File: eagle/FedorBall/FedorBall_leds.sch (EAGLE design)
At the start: 8 parts, among them U1 TLC5940-NT, U2 TLC5940-NT, U3 TLC5940-NT, U4 TLC5940-NT

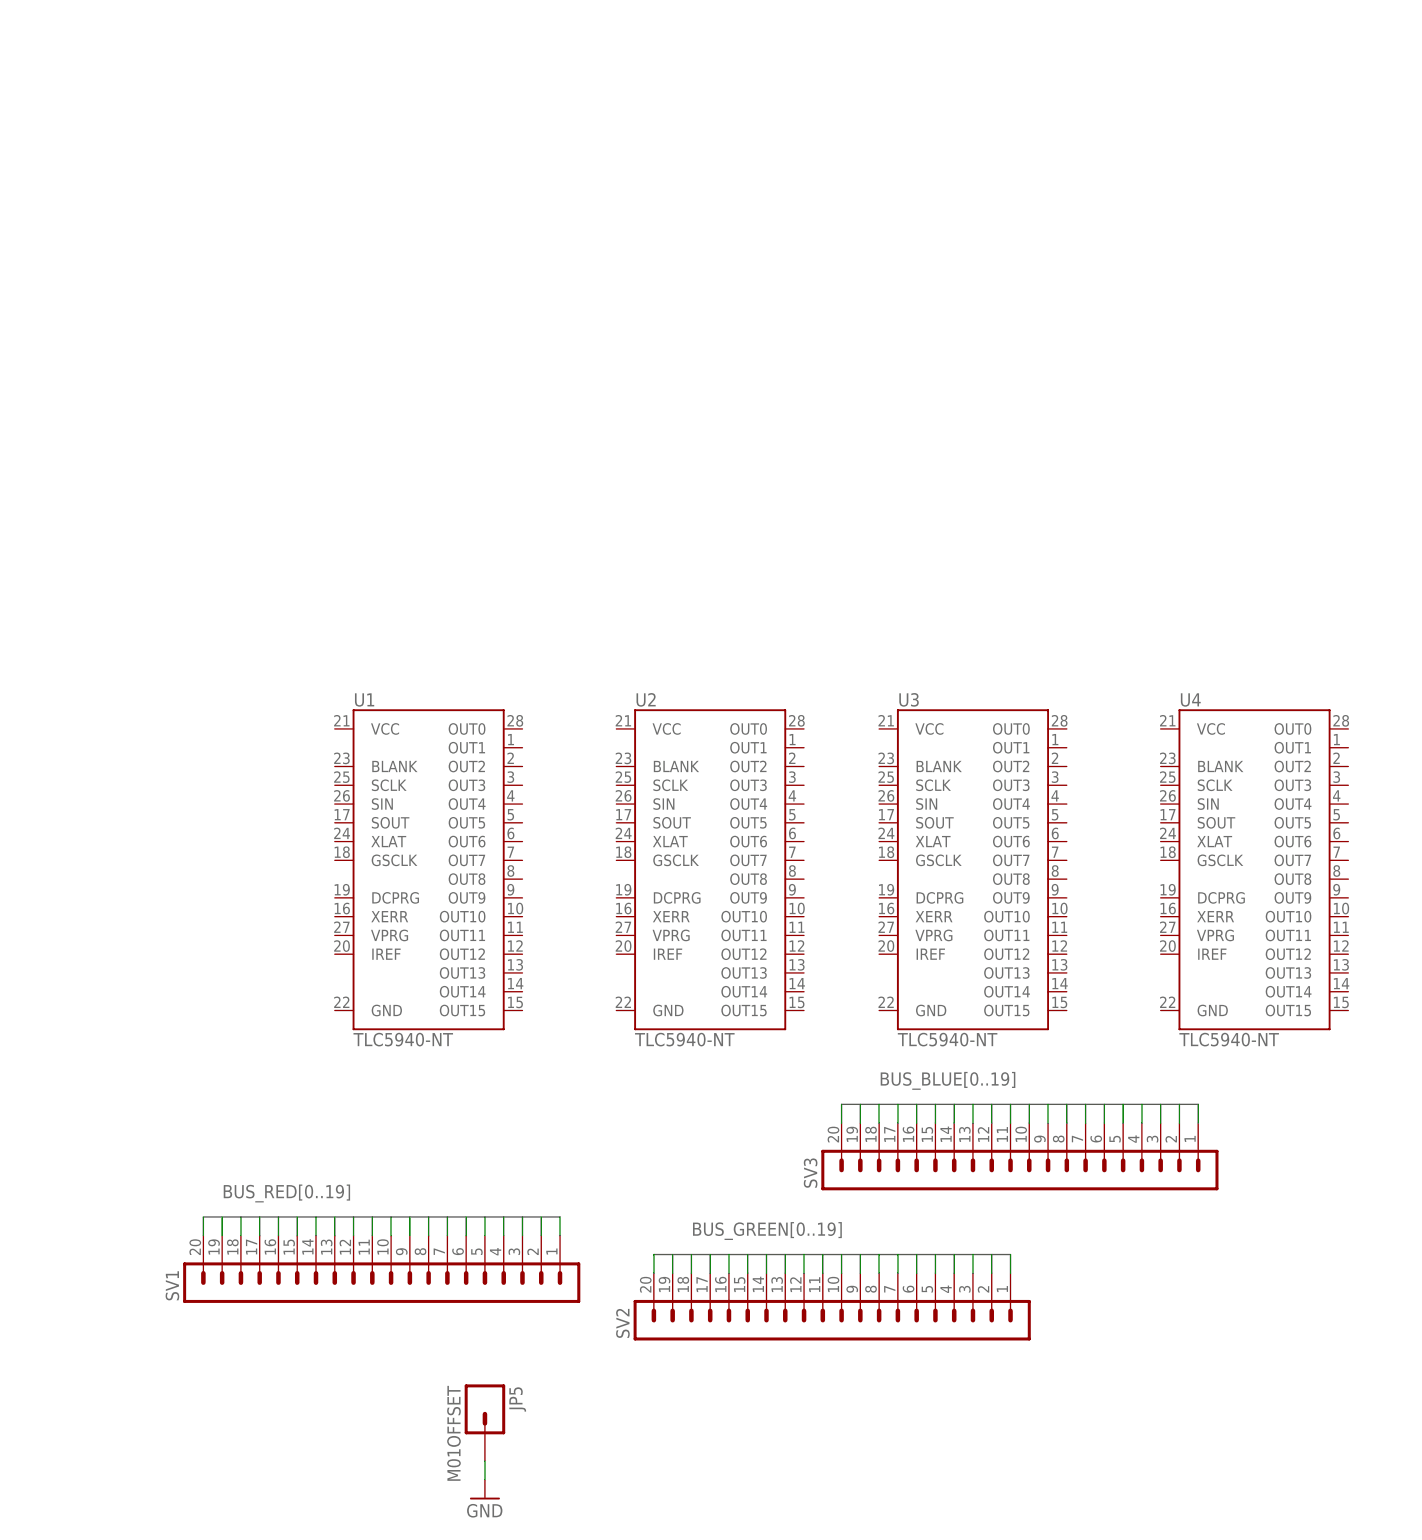
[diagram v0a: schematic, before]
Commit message: continue implementing leds driver scheme
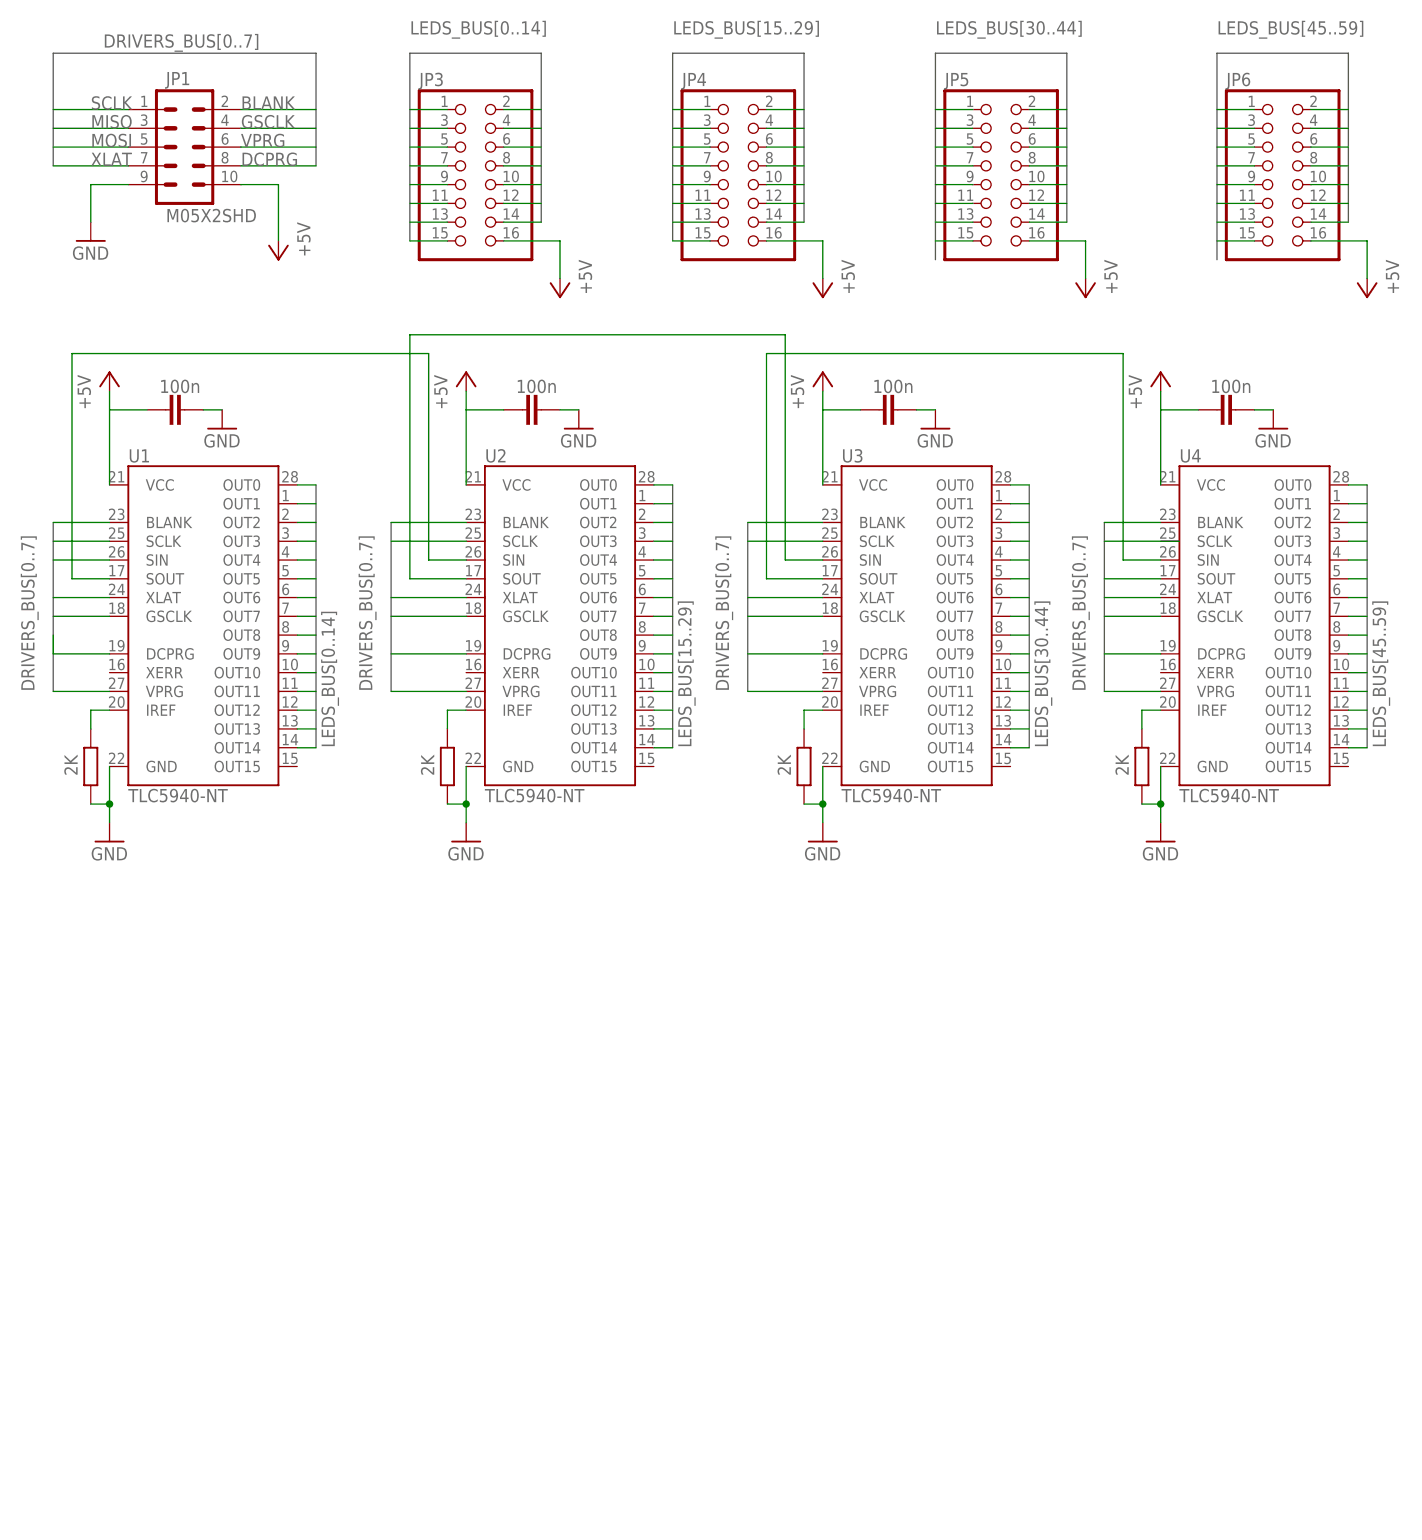
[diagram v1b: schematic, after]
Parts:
- removed SV1, SV2, SV3: (no value), con-lstb:MA20-1L
- added C1, C2, C3, C4: 100n, rcl:C-EU025-024X044
- added JP1: M05X2SHD, SparkFun:M05X2SHD
- added JP3, JP4, JP6: (no value), pinhead:PINHD-2X8
- added R1, R2, R3, R4: 2K, resistor:R-EU_0204/5
- JP5: value M01OFFSET -> (none); device SparkFun:M01OFFSET -> pinhead:PINHD-2X8
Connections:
- removed net BUS_BLUE0: SV3.1
- removed net BUS_BLUE1: SV3.2
- removed net BUS_BLUE10: SV3.11
- removed net BUS_BLUE11: SV3.12
- removed net BUS_BLUE12: SV3.13
- removed net BUS_BLUE13: SV3.14
- removed net BUS_BLUE14: SV3.15
- removed net BUS_BLUE15: SV3.16
- removed net BUS_BLUE16: SV3.17
- removed net BUS_BLUE17: SV3.18
- removed net BUS_BLUE18: SV3.19
- removed net BUS_BLUE19: SV3.20
- removed net BUS_BLUE2: SV3.3
- removed net BUS_BLUE3: SV3.4
- removed net BUS_BLUE4: SV3.5, SV3.6
- removed net BUS_BLUE6: SV3.7
- removed net BUS_BLUE7: SV3.8
- removed net BUS_BLUE8: SV3.9
- removed net BUS_BLUE9: SV3.10
- removed net BUS_GREEN0: SV2.1
- removed net BUS_GREEN1: SV2.2
- removed net BUS_GREEN10: SV2.11
- removed net BUS_GREEN11: SV2.12
- removed net BUS_GREEN12: SV2.13
- removed net BUS_GREEN13: SV2.14
- removed net BUS_GREEN14: SV2.15
- removed net BUS_GREEN15: SV2.16
- removed net BUS_GREEN16: SV2.17
- removed net BUS_GREEN17: SV2.18
- removed net BUS_GREEN18: SV2.19
- removed net BUS_GREEN19: SV2.20
- removed net BUS_GREEN3: SV2.3, SV2.4
- removed net BUS_GREEN4: SV2.5
- removed net BUS_GREEN5: SV2.6
- removed net BUS_GREEN6: SV2.7
- removed net BUS_GREEN7: SV2.8
- removed net BUS_GREEN8: SV2.9
- removed net BUS_GREEN9: SV2.10
- removed net BUS_RED0: SV1.1
- removed net BUS_RED1: SV1.2
- removed net BUS_RED10: SV1.11
- removed net BUS_RED11: SV1.12
- removed net BUS_RED12: SV1.13
- removed net BUS_RED13: SV1.14
- removed net BUS_RED14: SV1.15
- removed net BUS_RED15: SV1.16
- removed net BUS_RED16: SV1.17
- removed net BUS_RED17: SV1.18
- removed net BUS_RED18: SV1.19
- removed net BUS_RED19: SV1.20
- removed net BUS_RED2: SV1.3
- removed net BUS_RED3: SV1.4
- removed net BUS_RED4: SV1.5
- removed net BUS_RED5: SV1.6
- removed net BUS_RED6: SV1.7
- removed net BUS_RED7: SV1.8
- removed net BUS_RED8: SV1.9
- removed net BUS_RED9: SV1.10
- new net +5V: C1.1, C2.1, C3.1, C4.1, JP1.10, JP3.16, JP4.16, JP5.16, JP6.16, U1.VCC, U2.VCC, U3.VCC, U4.VCC
- new net DRIVERS_BUS0: JP1.2, U1.BLANK, U2.BLANK, U3.BLANK, U4.BLANK
- new net DRIVERS_BUS1: JP1.1, U1.SCLK, U2.SCLK, U3.SCLK
- new net DRIVERS_BUS2: JP1.5, U1.SIN
- new net DRIVERS_BUS3: JP1.3, U4.SOUT
- new net DRIVERS_BUS4: JP1.7, U1.XLAT, U2.XLAT, U3.XLAT, U4.XLAT
- new net DRIVERS_BUS5: JP1.4, U1.GSCLK, U2.GSCLK, U3.GSCLK, U4.GSCLK
- new net DRIVERS_BUS6: JP1.8, U1.DCPRG, U2.DCPRG, U3.DCPRG, U4.DCPRG
- new net DRIVERS_BUS7: JP1.6, U1.VPRG, U2.VPRG, U3.VPRG, U4.VPRG
- new net LEDS_BUS0: JP3.1, U1.OUT0
- new net LEDS_BUS1: JP3.3, U1.OUT1
- new net LEDS_BUS10: JP3.6, U1.OUT10
- new net LEDS_BUS11: JP3.8, U1.OUT11
- new net LEDS_BUS12: JP3.10, U1.OUT12
- new net LEDS_BUS13: JP3.12, U1.OUT13
- new net LEDS_BUS14: JP3.14, U1.OUT14
- new net LEDS_BUS15: JP4.1, U2.OUT0
- new net LEDS_BUS16: JP4.3, U2.OUT1
- new net LEDS_BUS17: JP4.5, U2.OUT2
- new net LEDS_BUS18: JP4.7, U2.OUT3
- new net LEDS_BUS19: JP4.9, U2.OUT4
- new net LEDS_BUS2: JP3.5, U1.OUT2
- new net LEDS_BUS20: JP4.11, U2.OUT5
- new net LEDS_BUS21: JP4.13, U2.OUT6
- new net LEDS_BUS22: JP4.15, U2.OUT7
- new net LEDS_BUS23: JP4.2, U2.OUT8
- new net LEDS_BUS24: JP4.4, U2.OUT9
- new net LEDS_BUS25: JP4.6, U2.OUT10
- new net LEDS_BUS26: JP4.8, U2.OUT11
- new net LEDS_BUS27: JP4.10, U2.OUT12
- new net LEDS_BUS28: JP4.12, U2.OUT13
- new net LEDS_BUS29: JP4.14, U2.OUT14
- new net LEDS_BUS3: JP3.7, U1.OUT3
- new net LEDS_BUS30: JP5.1, U3.OUT0
- new net LEDS_BUS31: JP5.3, U3.OUT1
- new net LEDS_BUS32: JP5.5, U3.OUT2
- new net LEDS_BUS33: JP5.7, U3.OUT3
- new net LEDS_BUS34: JP5.9, U3.OUT4
- new net LEDS_BUS35: JP5.11, U3.OUT5
- new net LEDS_BUS36: JP5.13, U3.OUT6
- new net LEDS_BUS37: JP5.15, U3.OUT7
- new net LEDS_BUS38: JP5.2, U3.OUT8
- new net LEDS_BUS39: JP5.4, U3.OUT9
- new net LEDS_BUS4: JP3.9, U1.OUT4
- new net LEDS_BUS40: JP5.6, U3.OUT10
- new net LEDS_BUS41: JP5.8, U3.OUT11
- new net LEDS_BUS42: JP5.10, U3.OUT12
- new net LEDS_BUS43: JP5.12, U3.OUT13
- new net LEDS_BUS44: JP5.14, U3.OUT14
- new net LEDS_BUS45: JP6.1, U4.OUT0
- new net LEDS_BUS46: JP6.3, U4.OUT1
- new net LEDS_BUS47: JP6.5, U4.OUT2
- new net LEDS_BUS48: JP6.7, U4.OUT3
- new net LEDS_BUS49: JP6.9, U4.OUT4
- new net LEDS_BUS5: JP3.11, U1.OUT5
- new net LEDS_BUS50: JP6.11, U4.OUT5
- new net LEDS_BUS51: JP6.13, U4.OUT6
- new net LEDS_BUS52: JP6.15, U4.OUT7
- new net LEDS_BUS53: JP6.2, U4.OUT8
- new net LEDS_BUS54: JP6.4, U4.OUT9
- new net LEDS_BUS55: JP6.6, U4.OUT10
- new net LEDS_BUS56: JP6.8, U4.OUT11
- new net LEDS_BUS57: JP6.10, U4.OUT12
- new net LEDS_BUS58: JP6.12, U4.OUT13
- new net LEDS_BUS59: JP6.14, U4.OUT14
- new net LEDS_BUS6: JP3.13, U1.OUT6
- new net LEDS_BUS7: JP3.15, U1.OUT7
- new net LEDS_BUS8: JP3.2, U1.OUT8
- new net LEDS_BUS9: JP3.4, U1.OUT9
- new net N$1: U1.SOUT, U2.SIN
- new net N$2: U2.SOUT, U3.SIN
- new net N$3: U3.SOUT, U4.SIN
- new net N$4: R2.2, U1.IREF
- new net N$5: R4.2, U2.IREF
- new net N$6: R3.2, U3.IREF
- new net N$7: R1.2, U4.IREF
- net GND: now also C1.2, C2.2, C3.2, C4.2, JP1.9, R1.1, R2.1, R3.1, R4.1, U1.GND, U2.GND, U3.GND, U4.GND; no longer JP5.1
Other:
- note added: "BLANK"
- note added: "DCPRG"
- note added: "GSCLK"
- note added: "MISO"
- note added: "MOSI"
- note added: "SCLK"
- note added: "VPRG"
- note added: "XLAT"
- moved on the sheet: U1, U2, U3, U4

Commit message: update scheme
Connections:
- net +5V: now also JP1.2; no longer JP1.10
- net DRIVERS_BUS0: now also JP1.6; no longer JP1.2
- net DRIVERS_BUS1: now also JP1.10; no longer JP1.1
- net DRIVERS_BUS2: now also JP1.9; no longer JP1.5
- net DRIVERS_BUS3: now also JP1.8; no longer JP1.3
- net DRIVERS_BUS4: now also JP1.3; no longer JP1.7
- net DRIVERS_BUS5: now also JP1.7; no longer JP1.4
- net DRIVERS_BUS6: now also JP1.4; no longer JP1.8
- net DRIVERS_BUS7: now also JP1.5; no longer JP1.6
- net GND: now also JP1.1; no longer JP1.9
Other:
- note added: "SIN"
- note added: "SOUT"
- note removed: "MISO"
- note removed: "MOSI"
- moved on the sheet: JP1
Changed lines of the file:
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@@
 <part name="P+8" library="supply1" deviceset="+5V" device=""/>
 <part name="P+9" library="supply1" deviceset="+5V" device=""/>
-<part name="P+10" library="supply1" deviceset="+5V" device=""/>
-<part name="GND5" library="supply1" deviceset="GND" device=""/>
 <part name="C1" library="rcl" deviceset="C-EU" device="025-024X044" value="100n"/>
 <part name="C2" library="rcl" deviceset="C-EU" device="025-024X044" value="100n"/>
@@
 <part name="GND8" library="supply1" deviceset="GND" device=""/>
 <part name="GND9" library="supply1" deviceset="GND" device=""/>
+<part name="P+1" library="supply1" deviceset="+5V" device=""/>
+<part name="GND5" library="supply1" deviceset="GND" device=""/>
 </parts>
 <sheets>
 <sheet>
 <plain>
-<text x="-12.7" y="175.26" size="1.778" layer="95">SCLK</text>
-<text x="-12.7" y="172.72" size="1.778" layer="95">MISO</text>
-<text x="-12.7" y="170.18" size="1.778" layer="95">MOSI</text>
-<text x="-12.7" y="167.64" size="1.778" layer="95">XLAT</text>
-<text x="7.62" y="175.26" size="1.778" layer="95">BLANK</text>
-<text x="7.62" y="172.72" size="1.778" layer="95">GSCLK</text>
-<text x="7.62" y="170.18" size="1.778" layer="95">VPRG</text>
+<text x="-15.24" y="167.64" size="1.778" layer="95">XLAT</text>
+<text x="-15.24" y="165.1" size="1.778" layer="95">VPRG</text>
+<text x="-15.24" y="162.56" size="1.778" layer="95">GSCLK</text>
+<text x="-15.24" y="160.02" size="1.778" layer="95">SIN</text>
 <text x="7.62" y="167.64" size="1.778" layer="95">DCPRG</text>
+<text x="7.62" y="165.1" size="1.778" layer="95">BLANK</text>
+<text x="7.62" y="162.56" size="1.778" layer="95">SOUT</text>
+<text x="7.62" y="160.02" size="1.778" layer="95">SCLK</text>
 </plain>
 <instances>
@@
 <instance part="U3" gate="G$1" x="99.06" y="106.68"/>
 <instance part="U4" gate="G$1" x="144.78" y="106.68"/>
-<instance part="JP1" gate="G$1" x="0" y="170.18"/>
+<instance part="JP1" gate="G$1" x="0" y="165.1"/>
 <instance part="JP3" gate="A" x="38.1" y="167.64"/>
 <instance part="JP4" gate="A" x="73.66" y="167.64"/>
@@
 <instance part="P+8" gate="1" x="86.36" y="139.7"/>
 <instance part="P+9" gate="1" x="132.08" y="139.7"/>
-<instance part="P+10" gate="1" x="12.7" y="154.94" rot="R180"/>
-<instance part="GND5" gate="1" x="-12.7" y="157.48"/>
 <instance part="C1" gate="G$1" x="-2.54" y="134.62" smashed="yes" rot="R90">
 <attribute name="VALUE" x="2.159" y="138.684" size="1.778" layer="96" rot="R180"/>
@@
 <instance part="GND8" gate="1" x="101.6" y="132.08"/>
 <instance part="GND9" gate="1" x="147.32" y="132.08"/>
+<instance part="P+1" gate="1" x="17.78" y="182.88"/>
+<instance part="GND5" gate="1" x="-17.78" y="182.88" rot="R180"/>
 </instances>
 <busses>
@@
 <bus name="DRIVERS_BUS[0..7]">
 <segment>
+<wire x1="76.2" y1="119.38" x2="76.2" y2="96.52" width="0.762" layer="92"/>
+<label x="73.66" y="96.52" size="1.778" layer="95" rot="R90"/>
+</segment>
+<segment>
+<wire x1="27.94" y1="119.38" x2="27.94" y2="96.52" width="0.762" layer="92"/>
+<label x="25.4" y="96.52" size="1.778" layer="95" rot="R90"/>
+</segment>
+<segment>
 <wire x1="-17.78" y1="119.38" x2="-17.78" y2="96.52" width="0.762" layer="92"/>
 <label x="-20.32" y="96.52" size="1.778" layer="95" rot="R90"/>
-<wire x1="27.94" y1="119.38" x2="27.94" y2="96.52" width="0.762" layer="92"/>
-<wire x1="76.2" y1="119.38" x2="76.2" y2="96.52" width="0.762" layer="92"/>
+</segment>
+<segment>
 <wire x1="124.46" y1="119.38" x2="124.46" y2="96.52" width="0.762" layer="92"/>
-<label x="25.4" y="96.52" size="1.778" layer="95" rot="R90"/>
-<label x="73.66" y="96.52" size="1.778" layer="95" rot="R90"/>
 <label x="121.92" y="96.52" size="1.778" layer="95" rot="R90"/>
-<label x="10.16" y="185.42" size="1.778" layer="95" rot="R180"/>
-<wire x1="-17.78" y1="167.64" x2="-17.78" y2="182.88" width="0.762" layer="92"/>
-<wire x1="-17.78" y1="182.88" x2="17.78" y2="182.88" width="0.762" layer="92"/>
-<wire x1="17.78" y1="182.88" x2="17.78" y2="167.64" width="0.762" layer="92"/>
+</segment>
+<segment>
+<wire x1="-17.78" y1="167.64" x2="-17.78" y2="154.94" width="0.762" layer="92"/>
+<wire x1="-17.78" y1="154.94" x2="17.78" y2="154.94" width="0.762" layer="92"/>
+<wire x1="17.78" y1="154.94" x2="17.78" y2="167.64" width="0.762" layer="92"/>
 </segment>
 </bus>
@@
 </segment>
 <segment>
-<pinref part="JP1" gate="G$1" pin="10"/>
-<pinref part="P+10" gate="1" pin="+5V"/>
-<wire x1="7.62" y1="165.1" x2="12.7" y2="165.1" width="0.1524" layer="91"/>
-<wire x1="12.7" y1="165.1" x2="12.7" y2="157.48" width="0.1524" layer="91"/>
+<pinref part="JP1" gate="G$1" pin="2"/>
+<wire x1="7.62" y1="170.18" x2="17.78" y2="170.18" width="0.1524" layer="91"/>
+<wire x1="17.78" y1="170.18" x2="17.78" y2="180.34" width="0.1524" layer="91"/>
+<pinref part="P+1" gate="1" pin="+5V"/>
 </segment>
 </net>
@@
 </segment>
 <segment>
-<pinref part="GND5" gate="1" pin="GND"/>
-<wire x1="-12.7" y1="160.02" x2="-12.7" y2="165.1" width="0.1524" layer="91"/>
-<pinref part="JP1" gate="G$1" pin="9"/>
-<wire x1="-12.7" y1="165.1" x2="-7.62" y2="165.1" width="0.1524" layer="91"/>
-</segment>
-<segment>
 <pinref part="C1" gate="G$1" pin="2"/>
 <pinref part="GND6" gate="1" pin="GND"/>
@@
 <pinref part="C4" gate="G$1" pin="2"/>
 <wire x1="147.32" y1="134.62" x2="144.78" y2="134.62" width="0.1524" layer="91"/>
+</segment>
+<segment>
+<pinref part="JP1" gate="G$1" pin="1"/>
+<wire x1="-7.62" y1="170.18" x2="-17.78" y2="170.18" width="0.1524" layer="91"/>
+<wire x1="-17.78" y1="170.18" x2="-17.78" y2="180.34" width="0.1524" layer="91"/>
+<pinref part="GND5" gate="1" pin="GND"/>
 </segment>
 </net>
@@
 </segment>
 <segment>
-<pinref part="JP1" gate="G$1" pin="2"/>
-<wire x1="7.62" y1="175.26" x2="17.78" y2="175.26" width="0.1524" layer="91"/>
+<pinref part="JP1" gate="G$1" pin="6"/>
+<wire x1="7.62" y1="165.1" x2="17.78" y2="165.1" width="0.1524" layer="91"/>
 </segment>
 </net>
@@
 </segment>
 <segment>
-<pinref part="JP1" gate="G$1" pin="1"/>
-<wire x1="-7.62" y1="175.26" x2="-17.78" y2="175.26" width="0.1524" layer="91"/>
+<pinref part="JP1" gate="G$1" pin="10"/>
+<wire x1="7.62" y1="160.02" x2="17.78" y2="160.02" width="0.1524" layer="91"/>
 </segment>
 </net>
@@
 </segment>
 <segment>
-<pinref part="JP1" gate="G$1" pin="5"/>
-<wire x1="-7.62" y1="170.18" x2="-17.78" y2="170.18" width="0.1524" layer="91"/>
+<pinref part="JP1" gate="G$1" pin="9"/>
+<wire x1="-7.62" y1="160.02" x2="-17.78" y2="160.02" width="0.1524" layer="91"/>
 </segment>
 </net>
@@
 </segment>
 <segment>
-<pinref part="JP1" gate="G$1" pin="3"/>
-<wire x1="-7.62" y1="172.72" x2="-17.78" y2="172.72" width="0.1524" layer="91"/>
+<pinref part="JP1" gate="G$1" pin="8"/>
+<wire x1="7.62" y1="162.56" x2="17.78" y2="162.56" width="0.1524" layer="91"/>
 </segment>
 </net>
@@
 </segment>
 <segment>
-<pinref part="JP1" gate="G$1" pin="7"/>
+<pinref part="JP1" gate="G$1" pin="3"/>
 <wire x1="-7.62" y1="167.64" x2="-17.78" y2="167.64" width="0.1524" layer="91"/>
 </segment>
@@
 </segment>
 <segment>
-<pinref part="JP1" gate="G$1" pin="4"/>
-<wire x1="7.62" y1="172.72" x2="17.78" y2="172.72" width="0.1524" layer="91"/>
+<pinref part="JP1" gate="G$1" pin="7"/>
+<wire x1="-7.62" y1="162.56" x2="-17.78" y2="162.56" width="0.1524" layer="91"/>
 </segment>
 </net>
@@
 </segment>
 <segment>
-<pinref part="JP1" gate="G$1" pin="8"/>
+<pinref part="JP1" gate="G$1" pin="4"/>
 <wire x1="7.62" y1="167.64" x2="17.78" y2="167.64" width="0.1524" layer="91"/>
 </segment>
@@
 </segment>
 <segment>
-<pinref part="JP1" gate="G$1" pin="6"/>
-<wire x1="7.62" y1="170.18" x2="17.78" y2="170.18" width="0.1524" layer="91"/>
-</segment>
-</net>
+<pinref part="JP1" gate="G$1" pin="5"/>
+<wire x1="-7.62" y1="165.1" x2="-17.78" y2="165.1" width="0.1524" layer="91"/>
+</segment>
+</net>
